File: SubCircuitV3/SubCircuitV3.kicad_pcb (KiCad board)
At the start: 2 copper layers, 121.4 x 121.2 mm, 52 parts, among them J1 JTAG, J10 ESC_POWER, J11 ESC_POWER, J12 ESC_POWER, J13 ESC_POWER, J14 FEMALE XT-60, J15 ESC PWM, J16 5S, J17 Water Sensor Input, J18 3S OUT, J19 2S OUT, J2 ESC PWM, J20 SWITCH, J21 U3V16F15, J22 CAM OUT, J3 ESC PWM, J4 ESC PWM, J5 ESC PWM, J6 ESC PWM, J7 3S, J8 ESC_POWER, J9 ESC_POWER, K1 G5Q-1A, Q1 NMOS, Q2 NMOS, Q3 NMOS, Q4 NMOS, Q5 NMOS, Q6 NMOS

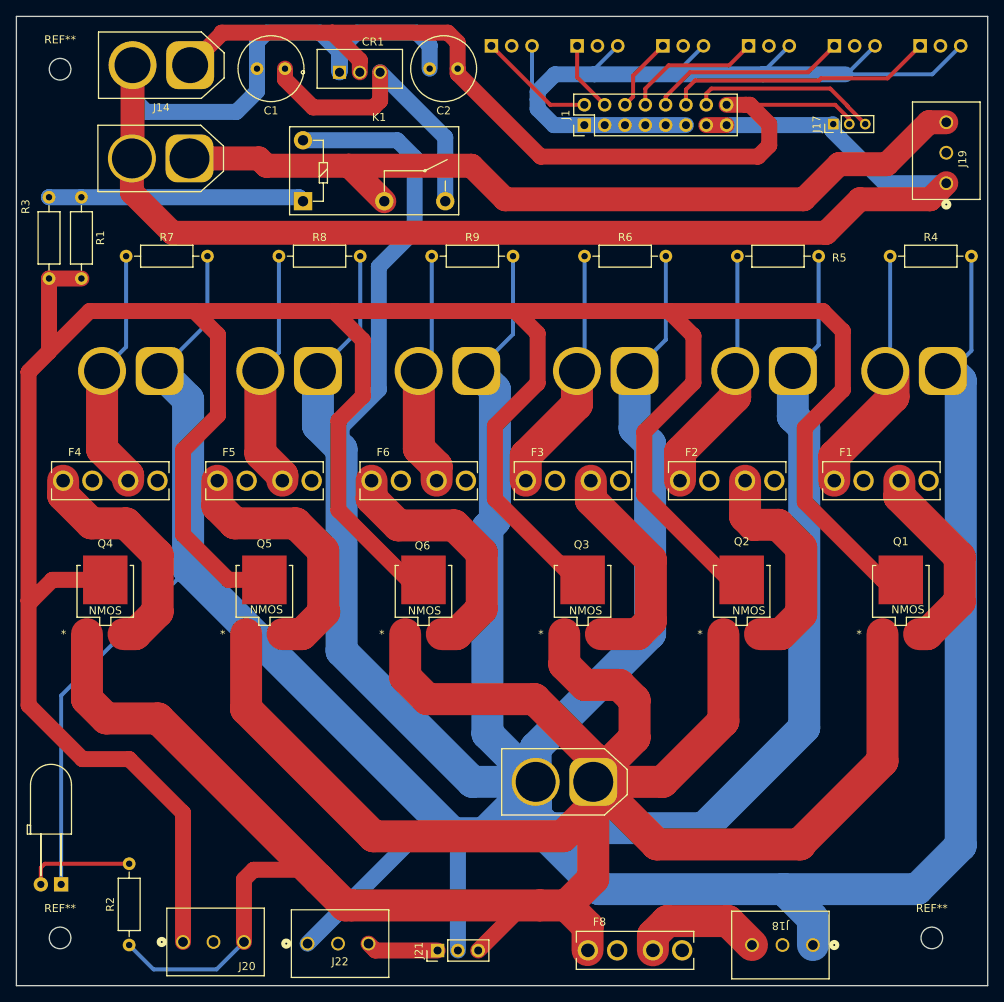
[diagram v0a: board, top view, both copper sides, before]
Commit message: Replaced old boost convertor with U3V70F15
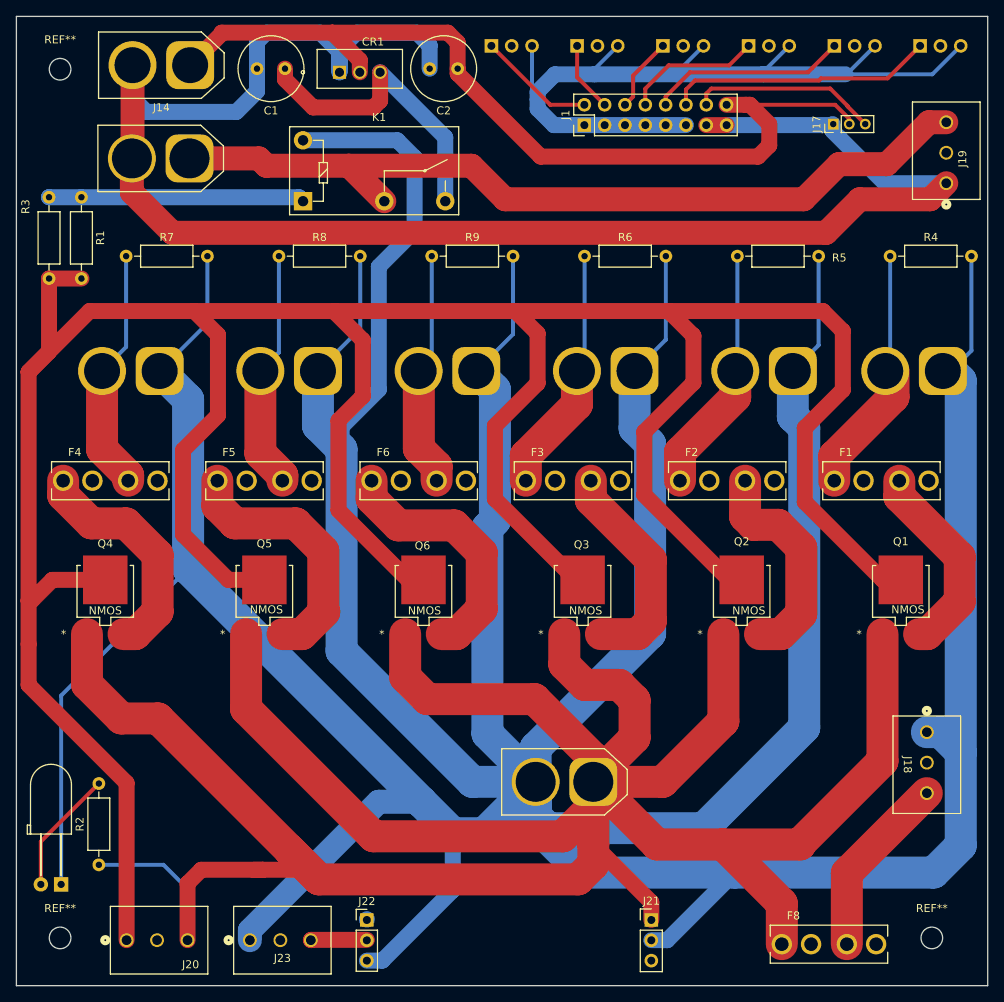
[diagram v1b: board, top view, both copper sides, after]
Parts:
- added J21: U3V16F15, Connector_PinHeader_2.54mm:PinHeader_1x03_P2.54mm_Vertical, F.Cu at (179.1, 138.5)
- moved J18 30.2 mm to (213.5, 115.0), turned to -90 degrees
- moved F8 24.3 mm to (201.3, 141.5)
- moved R2 10.7 mm to (110.0, 131.6)
- moved J22 9.63 mm to (143.5, 138.5), turned to 0 degrees
- moved J23 7.22 mm to (128.9, 141.0)
- moved J20 7.06 mm to (113.5, 141.0)
- renumbered J21 to J22, J22 to J23
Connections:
- J22 pad 1: Net-(J21-Pin_1) -> unconnected-(J22-Pin_1-Pad1)
- J22 pad 2: GND1 -> Net-(J22-Pin_2)
- J22 pad 3: +12V -> GND1
- J23 pad 3: Net-(J21-Pin_1) -> Net-(J22-Pin_2)
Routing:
- net GND1: track 724.5 -> 746.4 mm
- net +12V: track 364.2 -> 385.2 mm
- net Net-(J21-Pin_1): track 8.99 -> 0.00 mm
- net Net-(J22-Pin_2): track 0.00 -> 7.02 mm
- net /SG: track 428.3 -> 421.8 mm
- net Net-(J18-Pin_3): track 16.7 -> 23.0 mm
- net Net-(D1-A): track 13.3 -> 15.9 mm

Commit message: Adjusted spacing
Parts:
- moved J21 0.73 mm to (179.8, 138.5)
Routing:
- net GND1: track 746.4 -> 745.0 mm
- net +12V: track 385.2 -> 384.4 mm

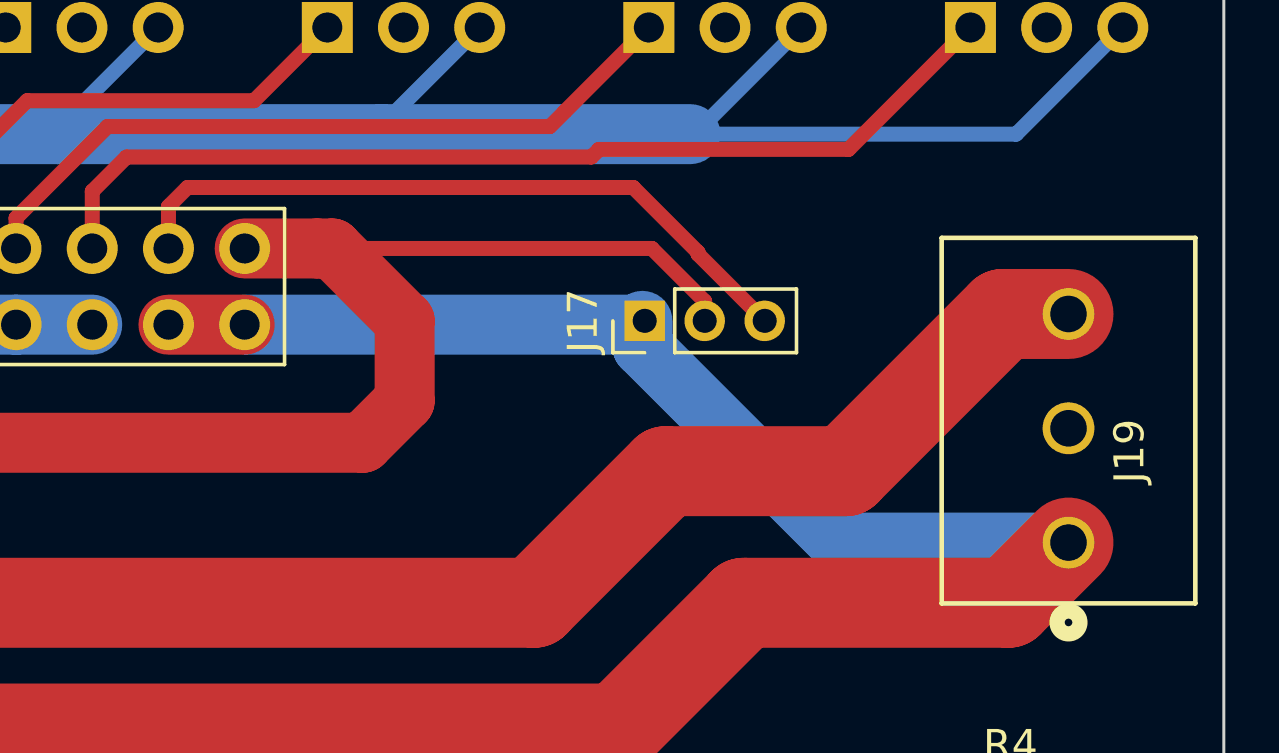
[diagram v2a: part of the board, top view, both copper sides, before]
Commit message: Updated WaterSensor pin size
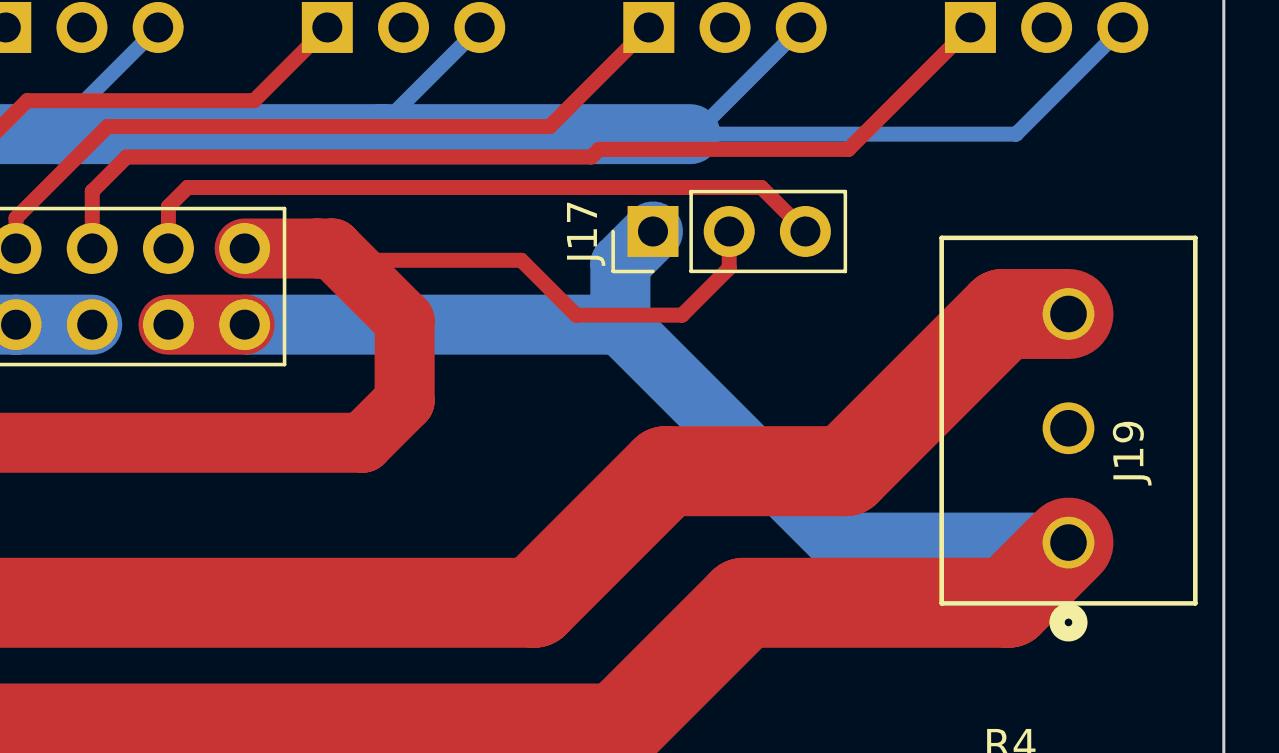
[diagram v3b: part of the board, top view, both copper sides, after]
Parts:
- J17: footprint Connector_PinHeader_2.00mm:PinHeader_1x03_P2.00mm_Vertical -> Connector_PinHeader_2.54mm:PinHeader_1x03_P2.54mm_Vertical
- moved J17 2.99 mm to (202.1, 36.0)
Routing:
- net GND2: track 218.7 -> 221.8 mm
- net Net-(CR1-OUTPUT): track 113.1 -> 114.8 mm
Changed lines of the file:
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@@
 		)
 	)
-	(footprint "Connector_PinHeader_2.00mm:PinHeader_1x03_P2.00mm_Vertical"
+	(footprint "Connector_PinHeader_2.54mm:PinHeader_1x03_P2.54mm_Vertical"
 		(layer "F.Cu")
-		(at 201.803 38.989 90)
-		(descr "Through hole straight pin header, 1x03, 2.00mm pitch, single row")
-		(tags "Through hole pin header THT 1x03 2.00mm single row")
+		(at 202.08 36.01 90)
+		(descr "Through hole straight pin header, 1x03, 2.54mm pitch, single row")
+		(tags "Through hole pin header THT 1x03 2.54mm single row")
 		(property "Reference" "J17"
-			(at 0 -2.06 90)
+			(at 0 -2.33 90)
 			(layer "F.SilkS")
 			(effects
@@
 		)
 		(property "Value" "Water Sensor Input"
-			(at 0 6.06 90)
+			(at 0 7.41 90)
 			(layer "F.Fab")
 			(effects
@@
 		(property "Datasheet" ""
 			(at 0 0 90)
+			(unlocked yes)
 			(layer "F.Fab")
 			(hide yes)
@@
 		(property "Description" ""
 			(at 0 0 90)
+			(unlocked yes)
 			(layer "F.Fab")
 			(hide yes)
@@
 		(attr through_hole)
 		(fp_line
-			(start -1.06 -1.06)
-			(end 0 -1.06)
+			(start -1.33 -1.33)
+			(end 0 -1.33)
 			(stroke
 				(width 0.12)
@@
 		)
 		(fp_line
-			(start -1.06 0)
-			(end -1.06 -1.06)
+			(start -1.33 0)
+			(end -1.33 -1.33)
 			(stroke
 				(width 0.12)
@@
 		)
 		(fp_line
-			(start 1.06 1)
-			(end 1.06 5.06)
+			(start 1.33 1.27)
+			(end 1.33 6.41)
 			(stroke
 				(width 0.12)
@@
 		)
 		(fp_line
-			(start -1.06 1)
-			(end 1.06 1)
+			(start -1.33 1.27)
+			(end 1.33 1.27)
 			(stroke
 				(width 0.12)
@@
 		)
 		(fp_line
-			(start -1.06 1)
-			(end -1.06 5.06)
+			(start -1.33 1.27)
+			(end -1.33 6.41)
 			(stroke
 				(width 0.12)
@@
 		)
 		(fp_line
-			(start -1.06 5.06)
-			(end 1.06 5.06)
+			(start -1.33 6.41)
+			(end 1.33 6.41)
 			(stroke
 				(width 0.12)
@@
 		)
 		(fp_line
-			(start 1.5 -1.5)
-			(end -1.5 -1.5)
+			(start 1.8 -1.8)
+			(end -1.8 -1.8)
 			(stroke
 				(width 0.05)
@@
 		)
 		(fp_line
-			(start -1.5 -1.5)
-			(end -1.5 5.5)
+			(start -1.8 -1.8)
+			(end -1.8 6.85)
 			(stroke
 				(width 0.05)
@@
 		)
 		(fp_line
-			(start 1.5 5.5)
-			(end 1.5 -1.5)
+			(start 1.8 6.85)
+			(end 1.8 -1.8)
 			(stroke
 				(width 0.05)
@@
 		)
 		(fp_line
-			(start -1.5 5.5)
-			(end 1.5 5.5)
+			(start -1.8 6.85)
+			(end 1.8 6.85)
 			(stroke
 				(width 0.05)
@@
 		)
 		(fp_line
-			(start 1 -1)
-			(end 1 5)
+			(start 1.27 -1.27)
+			(end 1.27 6.35)
 			(stroke
 				(width 0.1)
@@
 		)
 		(fp_line
-			(start -0.5 -1)
-			(end 1 -1)
+			(start -0.635 -1.27)
+			(end 1.27 -1.27)
 			(stroke
 				(width 0.1)
@@
 		)
 		(fp_line
-			(start -1 -0.5)
-			(end -0.5 -1)
+			(start -1.27 -0.635)
+			(end -0.635 -1.27)
 			(stroke
 				(width 0.1)
@@
 		)
 		(fp_line
-			(start 1 5)
-			(end -1 5)
+			(start 1.27 6.35)
+			(end -1.27 6.35)
 			(stroke
 				(width 0.1)
@@
 		)
 		(fp_line
-			(start -1 5)
-			(end -1 -0.5)
+			(start -1.27 6.35)
+			(end -1.27 -0.635)
 			(stroke
 				(width 0.1)
@@
 		)
 		(fp_text user "${REFERENCE}"
-			(at 0 2 0)
+			(at 0 2.54 180)
 			(layer "F.Fab")
 			(effects
@@
 		(pad "1" thru_hole rect
 			(at 0 0 90)
-			(size 1.35 1.35)
-			(drill 0.8)
+			(size 1.7 1.7)
+			(drill 1)
 			(layers "*.Cu" "*.Mask")
 			(remove_unused_layers no)
@@
 		)
 		(pad "2" thru_hole oval
-			(at 0 2 90)
-			(size 1.35 1.35)
-			(drill 0.8)
+			(at 0 2.54 90)
+			(size 1.7 1.7)
+			(drill 1)
 			(layers "*.Cu" "*.Mask")
 			(remove_unused_layers no)
@@
 		)
 		(pad "3" thru_hole oval
-			(at 0 4 90)
-			(size 1.35 1.35)
-			(drill 0.8)
+			(at 0 5.08 90)
+			(size 1.7 1.7)
+			(drill 1)
 			(layers "*.Cu" "*.Mask")
 			(remove_unused_layers no)
@@
 		)
 		(embedded_fonts no)
-		(model "${KICAD9_3DMODEL_DIR}/Connector_PinHeader_2.00mm.3dshapes/PinHeader_1x03_P2.00mm_Vertical.wrl"
+		(model "${KICAD9_3DMODEL_DIR}/Connector_PinHeader_2.54mm.3dshapes/PinHeader_1x03_P2.54mm_Vertical.wrl"
 			(offset
 				(xyz 0 0 0)
@@
 	)
 	(segment
-		(start 201.727 38.989)
-		(end 201.727 39.848908)
+		(start 200.994092 37.095908)
+		(end 202.08 36.01)
 		(width 2)
 		(layer "B.Cu")
@@
 	)
 	(segment
-		(start 188.468 39.116)
-		(end 201.676 39.116)
-		(width 2)
-		(layer "B.Cu")
-		(net 2)
-	)
-	(segment
-		(start 201.727 39.848908)
-		(end 208.258092 46.38)
-		(width 2)
-		(layer "B.Cu")
-		(net 2)
-	)
-	(segment
 		(start 130.941 27.559)
 		(end 129.77 28.73)
@@
 	)
 	(segment
+		(start 200.994092 39.116)
+		(end 200.994092 37.095908)
+		(width 2)
+		(layer "B.Cu")
+		(net 2)
+	)
+	(segment
 		(start 129.77 34.89)
 		(end 129.77 32.06)
@@
 	)
 	(segment
+		(start 200.994092 39.116)
+		(end 188.468 39.116)
+		(width 2)
+		(layer "B.Cu")
+		(net 2)
+	)
+	(segment
 		(start 140.081 29.718)
 		(end 142.24 27.559)
@@
 	)
 	(segment
+		(start 215.93 46.38)
+		(end 208.258092 46.38)
+		(width 2)
+		(layer "B.Cu")
+		(net 2)
+	)
+	(segment
 		(start 140.081 29.972)
 		(end 137.668 27.559)
@@
 	(segment
 		(start 208.258092 46.38)
-		(end 215.93 46.38)
+		(end 200.994092 39.116)
 		(width 2)
 		(layer "B.Cu")
@@
 	)
 	(segment
+		(start 203.05 38.8)
+		(end 204.62 37.23)
+		(width 0.5)
+		(layer "F.Cu")
+		(net 3)
+	)
+	(segment
 		(start 165.227 43.053)
 		(end 192.405 43.053)
@@
 	)
 	(segment
+		(start 191.783 36.97)
+		(end 197.69 36.97)
+		(width 0.5)
+		(layer "F.Cu")
+		(net 3)
+	)
+	(segment
 		(start 125.349 27.686)
 		(end 125.349 27.559)
@@
 	)
 	(segment
+		(start 191.389 36.576)
+		(end 191.783 36.97)
+		(width 0.5)
+		(layer "F.Cu")
+		(net 3)
+	)
+	(segment
 		(start 139.181 27.559)
 		(end 142.621 30.999)
@@
 	)
 	(segment
-		(start 190.881 36.576)
-		(end 202.042 36.576)
+		(start 204.62 37.23)
+		(end 204.62 36.01)
 		(width 0.5)
 		(layer "F.Cu")
@@
 	)
 	(segment
-		(start 191.389 36.576)
-		(end 190.881 36.576)
-		(width 2)
+		(start 199.52 38.8)
+		(end 203.05 38.8)
+		(width 0.5)
 		(layer "F.Cu")
 		(net 3)
 	)
 	(segment
-		(start 202.042 36.576)
-		(end 203.803 38.337)
-		(width 0.5)
+		(start 191.389 36.576)
+		(end 190.881 36.576)
+		(width 2)
 		(layer "F.Cu")
 		(net 3)
@@
 	)
 	(segment
-		(start 154.85 32.676)
-		(end 165.227 43.053)
-		(width 2)
+		(start 197.69 36.97)
+		(end 199.52 38.8)
+		(width 0.5)
 		(layer "F.Cu")
 		(net 3)
 	)
 	(segment
-		(start 203.803 38.337)
-		(end 203.803 38.989)
-		(width 0.5)
+		(start 154.85 32.676)
+		(end 165.227 43.053)
+		(width 2)
 		(layer "F.Cu")
 		(net 3)
@@
 	)
 	(segment
-		(start 185.928 36.576)
-		(end 185.928 35.179)
-		(width 0.5)
-		(layer "F.Cu")
-		(net 21)
-	)
-	(segment
-		(start 186.563 34.544)
-		(end 201.422 34.544)
-		(width 0.5)
-		(layer "F.Cu")
-		(net 21)
-	)
-	(segment
 		(start 185.928 35.179)
 		(end 186.563 34.544)
@@
 	)
 	(segment
-		(start 203.583 36.705)
-		(end 203.583 36.769)
+		(start 205.694 34.544)
+		(end 207.16 36.01)
 		(width 0.5)
 		(layer "F.Cu")
@@
 	)
 	(segment
-		(start 201.422 34.544)
-		(end 203.583 36.705)
+		(start 185.928 36.576)
+		(end 185.928 35.179)
 		(width 0.5)
 		(layer "F.Cu")
@@
 	)
 	(segment
-		(start 203.583 36.769)
-		(end 205.803 38.989)
+		(start 186.563 34.544)
+		(end 205.694 34.544)
 		(width 0.5)
 		(layer "F.Cu")
